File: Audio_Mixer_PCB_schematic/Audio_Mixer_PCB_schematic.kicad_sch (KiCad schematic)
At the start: 0 parts

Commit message: finalized spice diagram, started importing to kicad
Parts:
- added C1, C10, C11, C12, C13, C14, C15, C16, C17, C18, C19, C2, C20, C3, C4, C9: 470n, symbol ltspice:cap
- added R1, R2, R40, R41: 10k, symbol ltspice:res
- added R10: {(highpassP1 / 100) * 100k}, symbol ltspice:Res
- added R11: {(midpassP1 / 100) * 100k}, symbol ltspice:Res
- added R16, R17, R18, R19, R23, R24, R25, R5, R6, R7, R8: {summingR}, symbol ltspice:Res
- added R20: {(lowpassP / 100) * 100k}, symbol ltspice:Res
- added R21: {(highpassP / 100) * 100k}, symbol ltspice:Res
- added R22: {(midpassP / 100) * 100k}, symbol ltspice:Res
- added R26, R27, R28, R29, R3, R34, R35, R4: 3.3k, symbol ltspice:res
- added R30, R31, R32, R33, R36, R37, R38, R39: 68, symbol ltspice:res
- added R9: {(lowpassP1 / 100) * 100k}, symbol ltspice:Res
- added U1, U11, U12, U13, U14, U15, U16, U17, U2, U3, U4, U5, U6: Avol=1Meg GBW=10Meg Vos=0, symbol ltspice:OpAmps/UniversalOpAmp
- added V1, V2: AC 1, symbol ltspice:Voltage
- added V3: 12, symbol ltspice:Voltage
- added V5: -12, symbol ltspice:Voltage
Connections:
- new net: R11.1, R7.2
- new net: C20.1, R40.2, U16.2 (In-), U16.5 (OUT)
- new net: C20.2, R38.1, R39.2
- new net: C9.1, R27.1, U12.1 (In+)
- new net: C12.2, C14.2, R26.2, V1.1 (+)
- new net: C17.1, R37.2, U4.1 (In+)
- new net: C2.2, R3.1, R4.2
- new net: R23.2, R8.1, U5.5 (OUT)
- new net: R5.1, R6.1, R7.1, R8.2, U5.1 (In+)
- new net: C3.1, R35.2, U3.1 (In+)
- new net: C11.1, R29.2, U13.1 (In+)
- new net: R16.2, R20.1
- new net: R40.1, R41.1, U17.2 (In-)
- new net: R16.1, R17.1, R18.1, R19.2, U11.1 (In+)
- new net: R19.1, R24.2, U11.5 (OUT)
- new net: R34.1, R38.2, U3.2 (In-), U3.5 (OUT)
- new net: C13.2, C14.1, R30.2
- new net: C3.2, C4.1, R34.2
- new net: C10.2, R26.1, R27.2
- new net: R10.1, R6.2
- new net: R23.1, R24.1, R25.2, U6.1 (In+)
- new net: R28.1, R32.2, U13.2 (In-), U13.5 (OUT)
- new net: C11.2, C12.1, R28.2
- new net: R1.1, R2.1, U1.2 (In-)
- new net: R5.2, R9.1
- new net: C15.1, R33.1, U15.1 (In+)
- new net: R17.2, R21.1
- new net: C1.1, R4.1, U2.1 (In+)
- new net: C16.2, R32.1, R33.2
- new net: C16.1, R1.2, U15.2 (In-), U15.5 (OUT)
- new net: C19.1, R39.1, U16.1 (In+)
- new net: C13.1, R31.2, U14.1 (In+)
- new net: C17.2, C18.1, R36.2
- new net: R18.2, R22.1
- new net 0: C1.2, C15.2, C19.2, C9.2, R29.1, R31.1, R35.1, R37.1, U1.1 (In+), U11.2 (In-), U17.1 (In+), U5.2 (In-), U6.2 (In-), V1.2 (-), V2.2 (-), V3.2 (-), V5.2 (-)
- new net HighIn1: C18.2, C4.2, R3.2, V2.1 (+)
- new net HighOut: R10.2, R30.1, U14.2 (In-), U14.5 (OUT)
- new net HighOut1: R21.2, R36.1, U4.2 (In-), U4.5 (OUT)
- new net LowOut: C10.1, R9.2, U12.2 (In-), U12.5 (OUT)
- new net LowOut1: C2.1, R20.2, U2.2 (In-), U2.5 (OUT)
- new net MidOut: R11.2, R2.2, U1.5 (OUT)
- new net MidOut1: R22.2, R41.2, U17.5 (OUT)
- new net OPneg: U1.4 (V-), U11.4 (V-), U12.4 (V-), U13.4 (V-), U14.4 (V-), U15.4 (V-), U16.4 (V-), U17.4 (V-), U2.4 (V-), U3.4 (V-), U4.4 (V-), U5.4 (V-), U6.4 (V-), V5.1 (+)
- new net OPpos: U1.3 (V+), U11.3 (V+), U12.3 (V+), U13.3 (V+), U14.3 (V+), U15.3 (V+), U16.3 (V+), U17.3 (V+), U2.3 (V+), U3.3 (V+), U4.3 (V+), U5.3 (V+), U6.3 (V+), V3.1 (+)
- new net Out: R25.1, U6.5 (OUT)
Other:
- note added: ".ac dec 10 1 100k"
- note added: ".param highC=47n"
- note added: ".param highR=680"
- note added: ".param highpassP1=100"
- note added: ".param highpassP=100"
- note added: ".param lowC=470n"
- note added: ".param lowR=3.3k"
- note added: ".param lowpassP1=100"
- note added: ".param lowpassP=100"
- note added: ".param midpassP1=100"
- note added: ".param midpassP=100"
- note added: ".param summingR 100k"
- note added: "HIGHER PERCENT = LESS PASSTHROUGH LOWER PERCENT = MORE PASSTHROUGH"
- note added: "High pass - 5kHz"
- note added: "Low pass - 100Hz"
- note added: "Mid Band pass - 100Hz to 5khz"

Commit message: more sch stuff
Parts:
- removed C1, C17, C18, C19, C2, C20, C3, C4: 470n, symbol ltspice:cap
- removed R3, R34, R35, R4: 3.3k, symbol ltspice:res
- removed R36, R37, R38, R39: 68, symbol ltspice:res
- removed R40, R41: 10k, symbol ltspice:res
- removed U16, U17, U2, U3, U4: Avol=1Meg GBW=10Meg Vos=0, symbol ltspice:OpAmps/UniversalOpAmp
- removed V2: AC 1, symbol ltspice:Voltage
- added C21, C22, C23, C24, C5, C6, C7, C8: 470n, symbol ltspice:cap
- added R12, R13, R15, R43: 3.3k, symbol ltspice:res
- added R14, R42, R44, R45: 68, symbol ltspice:res
- added R46, R47: 10k, symbol ltspice:res
- added U10, U18, U7, U8, U9: Avol=1Meg GBW=10Meg Vos=0, symbol ltspice:OpAmps/UniversalOpAmp
- added V4: AC 1, symbol ltspice:Voltage
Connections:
- net 0: now also C21.2, C23.2, R14.1, R15.1, U18.1 (In+), V4.2 (-)
- net OPneg: now also U10.4 (V-), U18.4 (V-), U7.4 (V-), U8.4 (V-), U9.4 (V-)
- net OPpos: now also U10.3 (V+), U18.3 (V+), U7.3 (V+), U8.3 (V+), U9.3 (V+)
- net HighOut: no longer names the net of R10.2, R30.1, U14.2 (In-), U14.5 (OUT)
- net HighOut1: no longer names the net of R21.2
- net HighOut1: now also R42.1, U8.2 (In-), U8.5 (OUT)
- net LowOut: no longer names the net of C10.1, R9.2, U12.2 (In-), U12.5 (OUT)
- net LowOut1: no longer names the net of R20.2
- net LowOut1: now also C22.1, U7.2 (In-), U7.5 (OUT)
- net MidOut: no longer names the net of R11.2, R2.2, U1.5 (OUT)
- net MidOut1: no longer names the net of R22.2
- net MidOut1: now also R47.2, U18.5 (OUT)
- new net: C5.1, C7.2, R42.2
- new net: C5.2, C6.2, R12.2, V4.1 (+)
- new net: C23.1, R45.1, U10.1 (In+)
- new net: C24.2, R44.1, R45.2
- new net: C7.1, R14.2, U8.1 (In+)
- new net: C21.1, R13.1, U7.1 (In+)
- new net: C22.2, R12.1, R13.2
- new net: C8.1, R15.2, U9.1 (In+)
- new net: R46.1, R47.1, U18.2 (In-)
- new net: C24.1, R46.2, U10.2 (In-), U10.5 (OUT)
- new net: R43.1, R44.2, U9.2 (In-), U9.5 (OUT)
- new net: C6.1, C8.2, R43.2
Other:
- moved on the sheet: R10, R11, R23, R5, R6, R7, R8, R9, U5, V3, V5

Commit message: replaced a bunch of symbols of R, C, OPamps.overall just organizing better to export to pcb state.
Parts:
- removed U1, U12, U13, U14, U15, U5, U7: Avol=1Meg GBW=10Meg Vos=0, symbol ltspice:OpAmps/UniversalOpAmp
- removed V3: 12, symbol ltspice:Voltage
- removed V5: -12, symbol ltspice:Voltage
- added BT1: Battery_Cell, symbol Device:Battery_Cell
- added R3, R4: 10k, symbol Device:R
- added U1, U2, U3: TL074, symbol Amplifier_Operational:TL074
- C10, C11, C12, C13, C14, C15, C16, C21, C22, C23, C24, C5, C6, C7, C8, C9: symbol ltspice:cap -> Device:C
- R1, R12, R13, R14, R15, R2, R26, R27, R28, R29, R30, R31, R32, R33, R42, R43, R44, R45, R46, R47: symbol ltspice:res -> Device:R
- R10, R11, R16, R17, R18, R19, R20, R21, R22, R23, R24, R25, R5, R6, R7, R8, R9: symbol ltspice:Res -> Device:R
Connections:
- net at R11.2, R2.2: now also U2.1
- net at C9.1, R27.1: now also U1.3 (+)
- net at C10.1, R9.2: now also U1.1, U1.2 (-)
- net at R23.2, R8.1: now also U2.7
- net at R5.1, R6.1, R7.1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: now also U2.5 (+)
- net at C11.1, R29.2: now also U1.10 (+)
- net at R10.2, R30.1: now also U1.6 (-), U1.7
- net at R28.1, R32.2: now also U1.8, U1.9 (-)
- net at R1.1, R2.1: now also U2.2 (-)
- net at R46.1, R47.1, U18.2 (In-): now also U18.3 (V+)
- net at C15.1, R33.1: now also U1.12 (+)
- net at C16.1, R1.2: now also U1.13 (-), U1.14
- net at C13.1, R31.2: now also U1.5 (+)
- removed net OPneg: U10.4 (V-), U11.4 (V-), U18.4 (V-), U6.4 (V-), U8.4 (V-), U9.4 (V-)
- removed net OPpos: U10.3 (V+), U11.3 (V+), U18.3 (V+), U6.3 (V+), U8.3 (V+), U9.3 (V+)
- new net +9V: BT1.1 (+), R3.1, U1.4 (V+), U2.4 (V+), U3.4 (V+)
- new net GND: BT1.2 (-), R4.2, U1.11 (V-), U2.11 (V-), U3.11 (V-)
- new net VRef: R3.2, R4.1, U2.3 (+), U2.6 (-)
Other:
- moved on the sheet: U10, U11, U18, U6, U8, U9, V1, V4

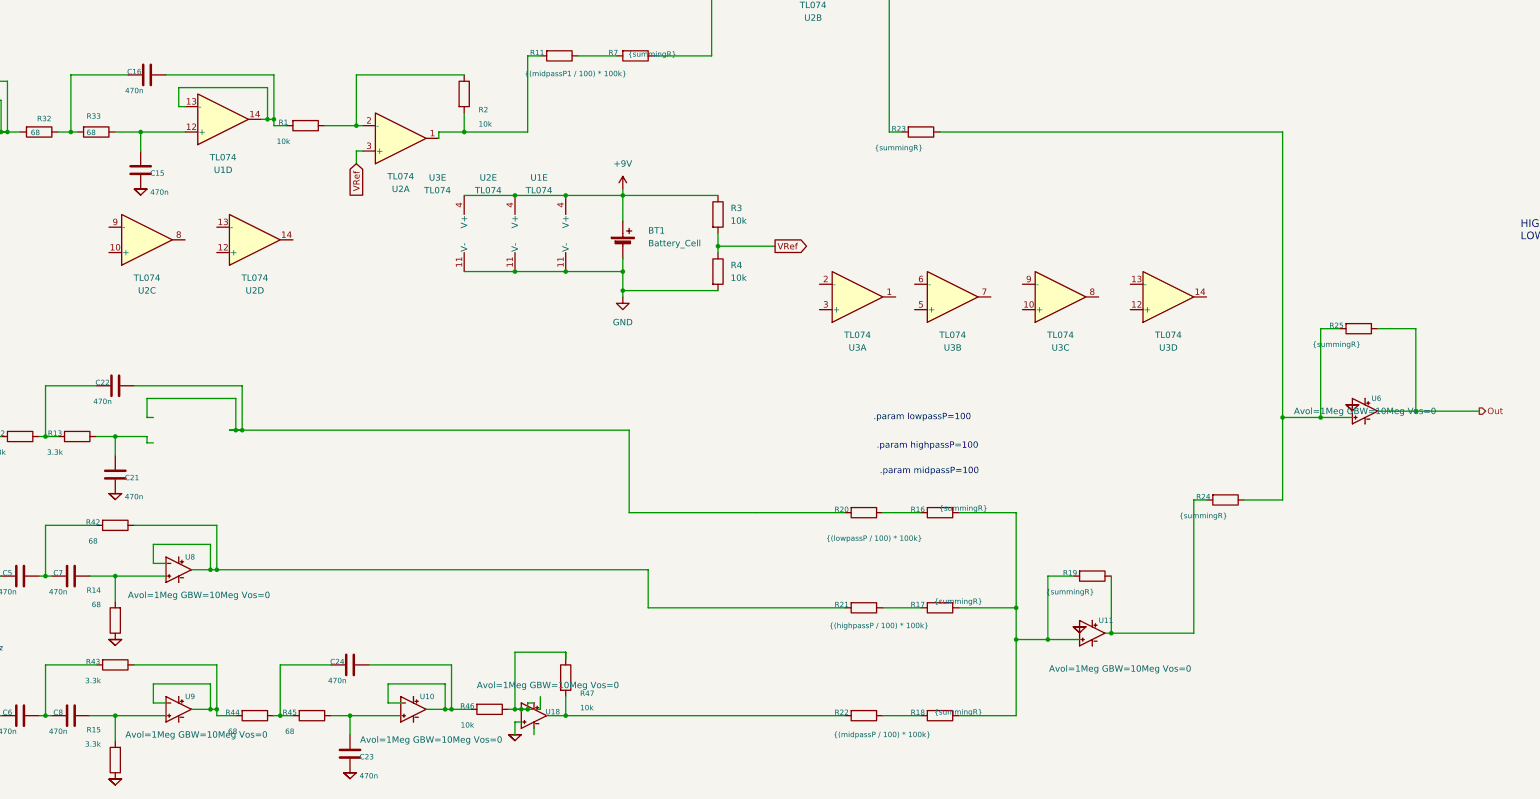
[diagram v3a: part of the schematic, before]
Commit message: finished adding op amp symbols
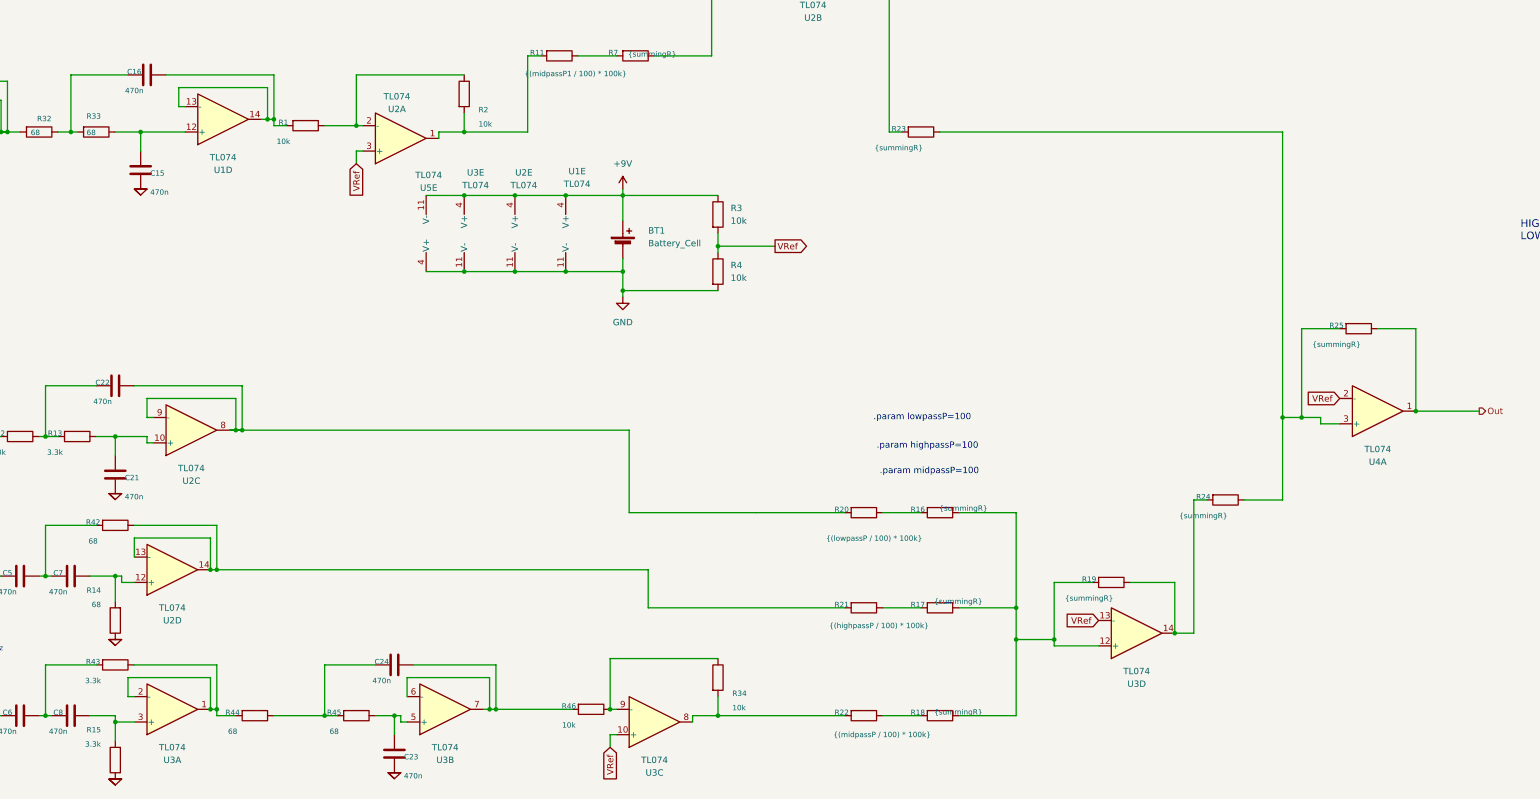
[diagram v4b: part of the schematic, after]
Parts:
- removed R47: 10k, symbol Device:R
- removed U10, U11, U18, U6, U8, U9: Avol=1Meg GBW=10Meg Vos=0, symbol ltspice:OpAmps/UniversalOpAmp
- added R34: 10k, symbol Device:R
- added U4, U5: TL074, symbol Amplifier_Operational:TL074
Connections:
- net +9V: now also U5.11 (V-)
- net GND: now also U5.4 (V+)
- net Out: now also U4.1
- net VRef: now also U3.10 (+), U3.13 (-), U4.2 (-)
- net at C23.1, R45.1: now also U3.5 (+)
- net at U2.12 (+): now also C7.1, R14.2
- net at U2.13 (-): now also R21.2, R42.1, U2.14
- net at C22.1, R20.2: now also U2.8, U2.9 (-)
- net at U2.10 (+): now also C21.1, R13.1
- net at R16.1, R17.1, R18.1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: now also U3.12 (+)
- net at R19.1, R24.2: now also U3.14
- net at R23.1, R24.1, R25.2: now also U4.3 (+)
- net at C8.1, R15.2: now also U3.3 (+)
- net at R46.1: now also U3.9 (-), R34.1
- net at C24.1, R46.2: now also U3.6 (-), U3.7
- net at R22.2: now also U3.8, R34.2
- net at R43.1, R44.2: now also U3.1, U3.2 (-)
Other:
- moved on the sheet: C23, C24, R45, R46, U2C, U2D, U3A, U3B, U3C, U3D

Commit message: audio jack for input done
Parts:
- removed V1, V4: AC 1, symbol ltspice:Voltage
- added C1, C2, C3: 10u, symbol Device:C
- added J1, J2: AudioJack3, symbol Connector_Audio:AudioJack3
- added RV1, RV2, RV3, RV4, RV5, RV6: R_Potentiometer, symbol Device:R_Potentiometer
- R10: value {(highpassP1 / 100) * 100k} -> 1k
- R11: value {(midpassP1 / 100) * 100k} -> 1k
- R20: value {(lowpassP / 100) * 100k} -> 1k
- R21: value {(highpassP / 100) * 100k} -> 1k
- R22: value {(midpassP / 100) * 100k} -> 1M
- R9: value {(lowpassP1 / 100) * 100k} -> 1M
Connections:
- net 0: no longer R14.1, R15.1, R29.1, R31.1
- net GND: now also C1.2, J1.S, J2.S
- net VRef: now also R14.1, R15.1, R22.2, R29.1, R31.1, R9.2, C1.1, RV1.1, RV2.1, RV3.1, RV4.1, RV5.1, RV6.1
- net at R7.2: now also RV3.2; no longer R11.1
- net at R2.2, U2.1: now also RV3.3; no longer R11.2
- net at C5.2, C6.2, R12.2: now also R22.1, C3.2
- net at C12.2, C14.2, R26.2: now also R9.1, C2.2
- net at R42.1, U2.13 (-), U2.14: now also RV5.3; no longer R21.2
- net at R16.2: now also RV4.2; no longer R20.1
- net at C22.1, U2.8, U2.9 (-): now also RV4.3; no longer R20.2
- net at C10.1, U1.1, U1.2 (-): now also RV1.3; no longer R9.2
- net at R6.2: now also RV2.2; no longer R10.1
- net at R30.1, U1.6 (-), U1.7: now also RV2.3; no longer R10.2
- net at R5.2: now also RV1.2; no longer R9.1
- net at R21.1: now also J2.R; no longer R17.2
- net at R34.2, U3.8: now also RV6.3; no longer R22.2
- net at R18.2: now also RV6.2; no longer R22.1
- new net: C2.1, R10.2, R11.2
- new net: C3.1, R20.2, R21.2
- new net: J1.R, R10.1
- new net: J1.T, R11.1
- new net: J2.T, R20.1
- new net: R17.2, RV5.2

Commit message: finished the sch for kicad. flipped summing op amps in lt spice to match the sch orientation
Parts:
- added C4: 10u, symbol Device:C
- added J3: AudioJack3, symbol Connector_Audio:AudioJack3
- added R35: 100k, symbol Device:R
- R16, R17, R18, R19, R23, R24, R25, R5, R6, R7, R8: value {summingR} -> 100k
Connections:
- net GND: now also J3.S, R35.2
- net VRef: now also U2.5 (+), U3.12 (+), U4.3 (+); no longer U2.6 (-), U3.13 (-), U4.2 (-)
- net at R5.1, R6.1, R7.1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: now also U2.6 (-); no longer U2.5 (+)
- net at R23.1, R24.1, R25.2: now also U4.2 (-); no longer U4.3 (+)
- net at R16.1, R17.1, R18.1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: now also U3.13 (-); no longer U3.12 (+)
- net Out: no longer names the net of R25.1, U4.1
- net Out: now also C4.1
- new net: C4.2, J3.R, J3.T, R35.1
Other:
- note removed: ".ac dec 10 1 100k"
- note removed: ".param highC=47n"
- note removed: ".param highR=680"
- note removed: ".param highpassP1=100"
- note removed: ".param highpassP=100"
- note removed: ".param lowC=470n"
- note removed: ".param lowR=3.3k"
- note removed: ".param lowpassP1=100"
- note removed: ".param lowpassP=100"
- note removed: ".param midpassP1=100"
- note removed: ".param midpassP=100"
- note removed: ".param summingR 100k"
